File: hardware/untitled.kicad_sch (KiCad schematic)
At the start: 25 parts, among them J1 D369-B66-NP4, U1 LM393, U2 LM393, U3 LM393, U4 MC78M12CDTG DPAK, U7 LM1117-5.0

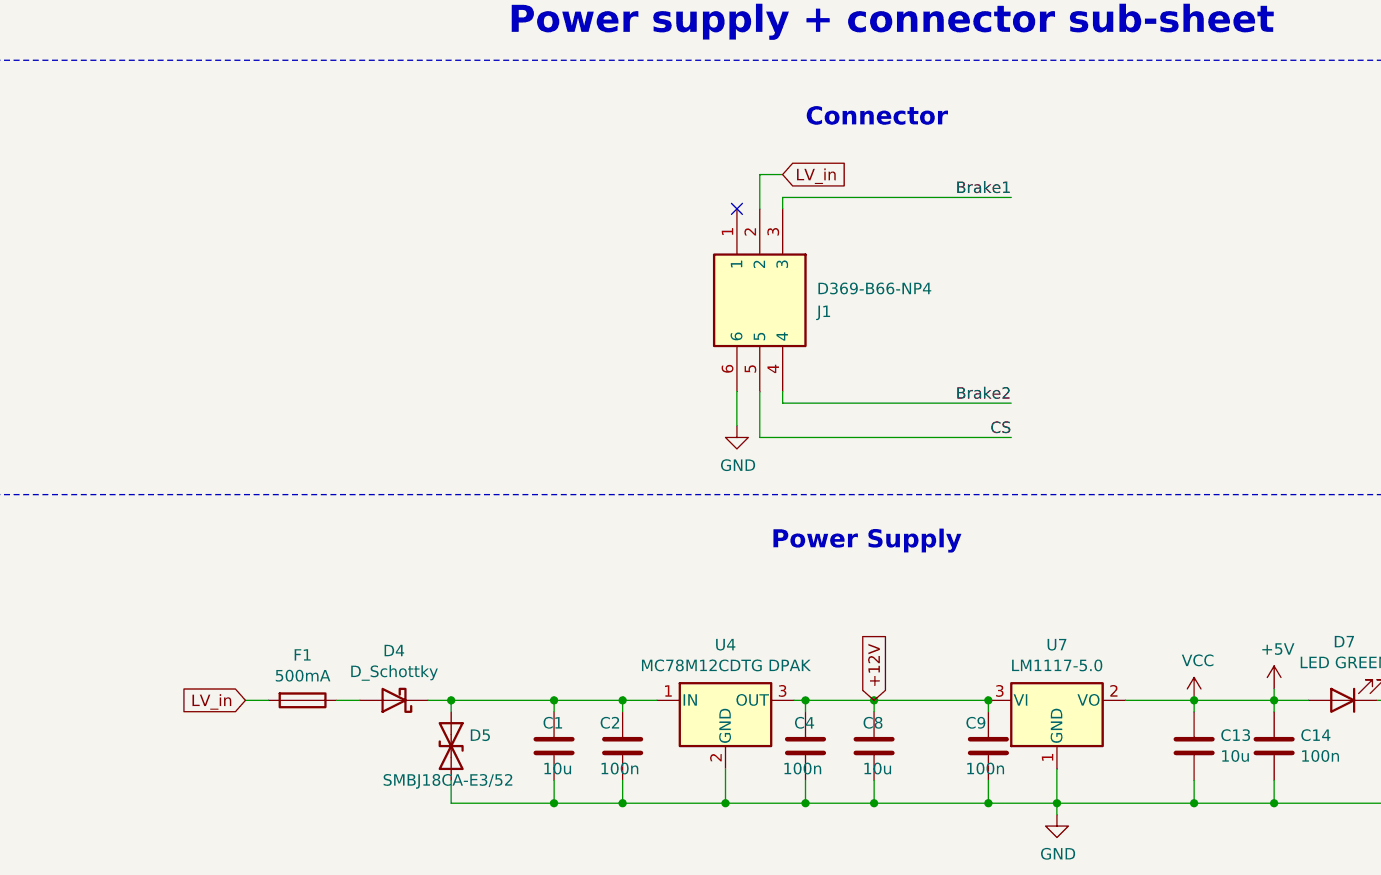
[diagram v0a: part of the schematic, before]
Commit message: Changed the connector
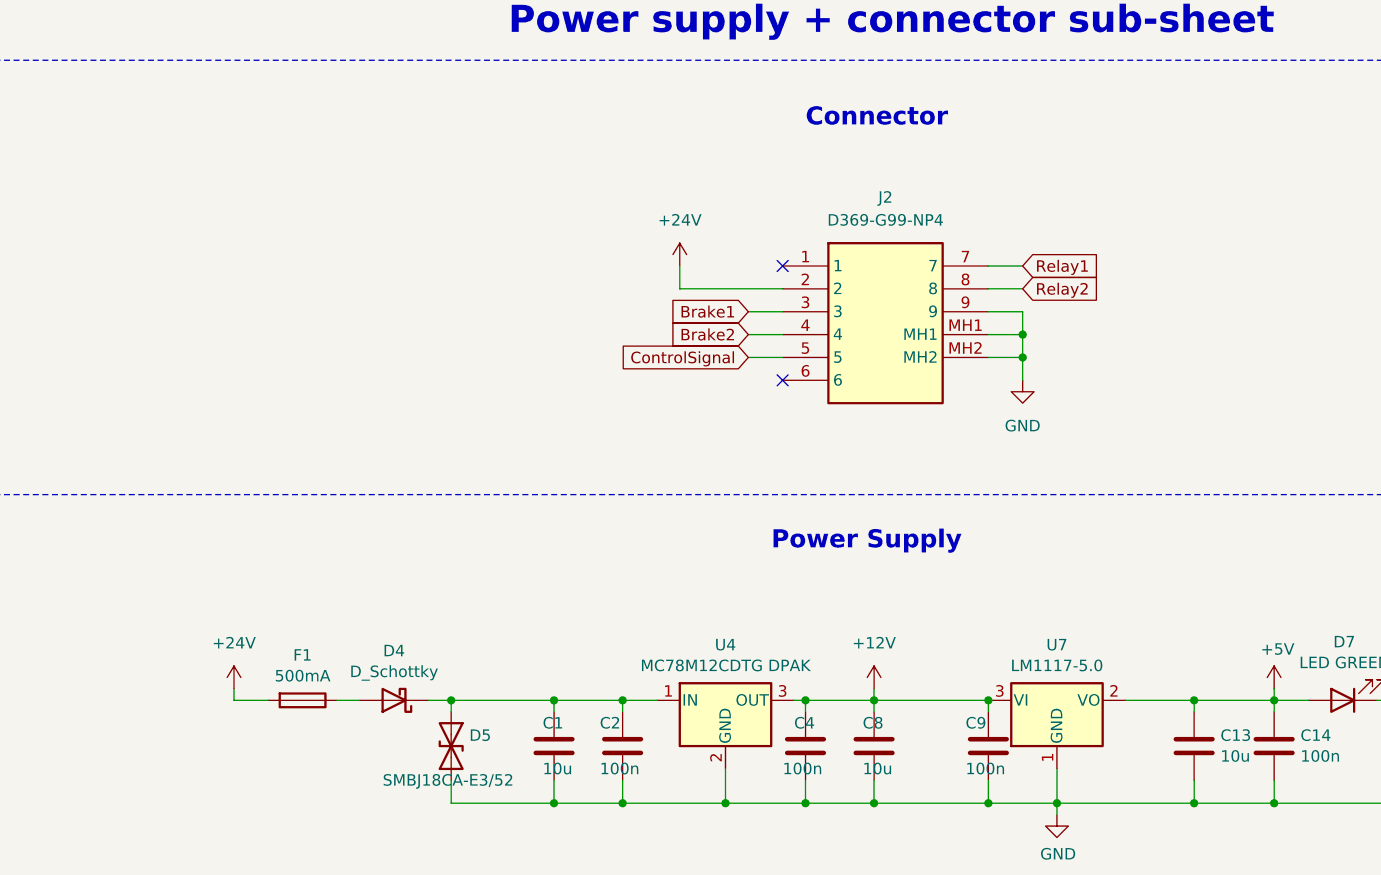
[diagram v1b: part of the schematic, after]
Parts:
- removed J1: D369-B66-NP4, D369B66NP4, symbol D369-B66-NP4:D369-B66-NP4
- added J2: D369-G99-NP4, D369G99NP4, symbol D369-G99-NP4:D369-G99-NP4
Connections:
- net Brake1: now also J2.3
- net Brake2: now also J2.4
- net GND: now also J2.9, J2.MH1, J2.MH2
- net LV_in renamed +24V
- net +24V: now also J2.2
- new net ControlSignal: J2.5
- new net Relay1: J2.7
- new net Relay2: J2.8
- no-connect marks 1 -> 2
